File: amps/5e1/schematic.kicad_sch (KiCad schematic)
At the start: 26 parts, among them T1 SE 5k:8

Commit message: Add: real tube pin numbers and readable valve glyphs on every schematic
Phase B of the drawing program. A factory service sheet numbers every tube
pin, because the number is what a technician puts a probe on. This corpus
printed none, and the numbers hidden in its symbols were positional
placeholders (P=1, G=2, K=3) that would have published a 6V6GT's plate as
pin 1 when it is pin 3.

1055 electrodes now carry the real number, 1027 lettered (27 are shared
filaments deduped, 1 dropped for want of clear space on the 6G2). Resolved per
instance from reference/tubes/<slug>.yaml through the same alias resolution the
layout renderer uses, so a 12AX7 section and a 6SL7 section each get their own
basing. A valve whose basing the corpus does not carry prints nothing rather
than a wrong number.

Section letters and basing units are now separate things, which cost a detour
worth recording. The RCA 12AX7-A sheet reads "Pin 1 - Plate of Unit No.2 ...
Pin 6 - Plate of Unit No.1", so unit numbering is not pin order; the 5Y3 and
GZ34 number their units in opposite pin order, so nothing positional can
express it. But the section LETTER is a designator, not a basing fact: this
corpus, like every technician, calls the first stage in signal order V1A, and
five amps' prose already did. On four amps the factory sheets put that first
stage on the other half -- the AA764's own schematic prints +200 V on pin 1 --
so those drawings now state their unit explicitly, each citing its source, and
no letter, netlist, parts list or layout comment changed. 183 layout comments
agree with the printed numbers, 0 disagree. A guard fires if two halves of one
bottle resolve to the same unit, which is exactly how this was found.

Glyphs: the cathode gains a bracket and filament hairpin so it can no longer be
confused with the plate bar, the pentode's screen sits on its own row, and a
rectifier draws as one envelope over its sections instead of two apparent
bottles. Line weights are scaled per sheet to a co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
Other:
- note added: "1"
- note added: "2"
- note added: "2,8"
- note added: "3"
- note added: "4"
- note added: "5"
- note added: "6"
- note added: "7"
- note added: "8"
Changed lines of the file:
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@@
   (wire (pts (xy 41.4116 30.278) (xy 41.4116 38.278))
     (stroke (width 0) (type default)))
-  (junction (at 41.4116 38.278) (diameter 0) (color 0 0 0 0))
+  (junction (at 41.4116 38.278) (diameter 1) (color 0 0 0 0))
   (symbol (lib_id "cx:R") (at 41.4116 42.088 0) (unit 1)
     (in_bom yes) (on_board yes)
@@
   (wire (pts (xy 52.8416 27.178) (xy 60.4616 27.178))
     (stroke (width 0) (type default)))
-  (junction (at 52.8416 27.178) (diameter 0) (color 0 0 0 0))
+  (junction (at 52.8416 27.178) (diameter 1) (color 0 0 0 0))
   (symbol (lib_id "cx:C") (at 64.2716 27.178 90) (unit 1)
     (in_bom yes) (on_board yes)
@@
   (wire (pts (xy 98.5616 45.898) (xy 98.5616 48.278))
     (stroke (width 0) (type default)))
-  (junction (at 98.5616 48.278) (diameter 0) (color 0 0 0 0))
+  (junction (at 98.5616 48.278) (diameter 1) (color 0 0 0 0))
   (symbol (lib_id "cx:R") (at 98.5616 52.088 0) (unit 1)
     (in_bom yes) (on_board yes)
@@
   (wire (pts (xy 98.5616 27.178) (xy 106.182 27.178))
     (stroke (width 0) (type default)))
-  (junction (at 98.5616 27.178) (diameter 0) (color 0 0 0 0))
+  (junction (at 98.5616 27.178) (diameter 1) (color 0 0 0 0))
   (symbol (lib_id "cx:C") (at 109.992 27.178 90) (unit 1)
     (in_bom yes) (on_board yes)
@@
   (wire (pts (xy 118.882 27.178) (xy 118.882 38.278))
     (stroke (width 0) (type default)))
-  (junction (at 118.882 38.278) (diameter 0) (color 0 0 0 0))
+  (junction (at 118.882 38.278) (diameter 1) (color 0 0 0 0))
   (symbol (lib_id "cx:R") (at 118.882 42.088 0) (unit 1)
     (in_bom yes) (on_board yes)
@@
   (wire (pts (xy 55.3816 111.078) (xy 68.0816 111.078))
     (stroke (width 0) (type default)))
-  (junction (at 55.3816 111.078) (diameter 0) (color 0 0 0 0))
-  (junction (at 68.0816 111.078) (diameter 0) (color 0 0 0 0))
+  (junction (at 55.3816 111.078) (diameter 1) (color 0 0 0 0))
+  (junction (at 68.0816 111.078) (diameter 1) (color 0 0 0 0))
   (symbol (lib_id "cx:C") (at 68.0816 114.888 0) (unit 1)
     (in_bom yes) (on_board yes)
@@
   (wire (pts (xy 91.1216 111.078) (xy 98.8816 111.078))
     (stroke (width 0) (type default)))
-  (junction (at 98.8816 111.078) (diameter 0) (color 0 0 0 0))
+  (junction (at 98.8816 111.078) (diameter 1) (color 0 0 0 0))
   (symbol (lib_id "cx:C") (at 98.8816 114.888 0) (unit 1)
     (in_bom yes) (on_board yes)
@@
   (wire (pts (xy 110.502 111.078) (xy 113.882 111.078))
     (stroke (width 0) (type default)))
-  (junction (at 113.882 111.078) (diameter 0) (color 0 0 0 0))
+  (junction (at 113.882 111.078) (diameter 1) (color 0 0 0 0))
   (symbol (lib_id "cx:C") (at 113.882 114.888 0) (unit 1)
     (in_bom yes) (on_board yes)
@@
   (global_label "B+3" (shape input) (at 113.882 107.518 90)
     (effects (font (size 1.27 1.27)) (justify left)))
+  (polyline (pts (xy 55.3816 95.978) (xy 56.3726 96.076) (xy 57.3256 96.365) (xy 58.2036 96.834) (xy 58.9736 97.466) (xy 59.6056 98.236) (xy 60.0746 99.114) (xy 60.3636 100.067) (xy 60.4616 101.058) (xy 60.3636 102.049) (xy 60.0746 103.002) (xy 59.6056 103.88) (xy 58.9736 104.65) (xy 58.2036 105.282) (xy 57.3256 105.751) (xy 56.3726 106.04) (xy 55.3816 106.138) (xy 42.6816 106.138) (xy 41.6906 106.04) (xy 40.7376 105.751) (xy 39.8596 105.282) (xy 39.0896 104.65) (xy 38.4576 103.88) (xy 37.9886 103.002) (xy 37.6996 102.049) (xy 37.6016 101.058) (xy 37.6996 100.067) (xy 37.9886 99.114) (xy 38.4576 98.236) (xy 39.0896 97.466) (xy 39.8596 96.834) (xy 40.7376 96.365) (xy 41.6906 96.076) (xy 42.6816 95.978) (xy 55.3816 95.978))
+    (stroke (width 0.3) (type default) (color 197 163 255 1)) (fill (type none)))
+  (polyline (pts (xy 40.7816 103.293) (xy 42.6816 101.693) (xy 49.0316 103.773) (xy 55.3816 101.693) (xy 57.2816 103.293))
+    (stroke (width 0.3) (type default) (color 197 163 255 1)) (fill (type none)))
+  (text "6" (at 53.6916 31.928 0)
+    (effects (font (size 1.1 1.1)) (justify left)))
+  (text "7" (at 45.8944 36.878 0)
+    (effects (font (size 1.1 1.1)) (justify left)))
+  (text "8" (at 53.6916 44.628 0)
+    (effects (font (size 1.1 1.1)) (justify left)))
+  (text "1" (at 99.4116 31.928 0)
+    (effects (font (size 1.1 1.1)) (justify left)))
+  (text "2" (at 91.6144 36.878 0)
+    (effects (font (size 1.1 1.1)) (justify left)))
+  (text "3" (at 99.4116 44.628 0)
+    (effects (font (size 1.1 1.1)) (justify left)))
+  (text "3" (at 129.892 31.293 0)
+    (effects (font (size 1.1 1.1)) (justify left)))
+  (text "5" (at 122.094 36.878 0)
+    (effects (font (size 1.1 1.1)) (justify left)))
+  (text "4" (at 134.942 35.608 0)
+    (effects (font (size 1.1 1.1)) (justify left)))
+  (text "8" (at 129.892 43.993 0)
+    (effects (font (size 1.1 1.1)) (justify left)))
+  (text "6" (at 43.5316 94.708 0)
+    (effects (font (size 1.1 1.1)) (justify left)))
+  (text "2,8" (at 43.5316 107.408 0)
+    (effects (font (size 1.1 1.1)) (justify left)))
+  (text "4" (at 56.2316 94.708 0)
+    (effects (font (size 1.1 1.1)) (justify left)))
   (text "Power supply — center-tapped HT · 5Y3GT full-wave · choke-filtered · heaters and PT primary omitted" (at 12.7 129.856 0)
     (effects (font (size 1.2 1.2)) (justify left)))

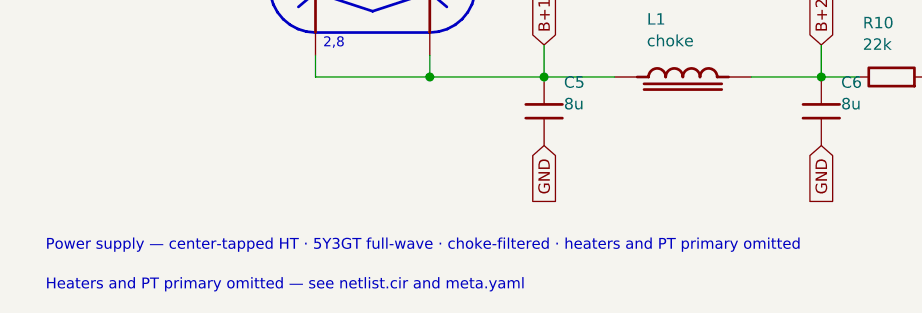
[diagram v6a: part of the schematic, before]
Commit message: Fix: schematic sheet notes no longer name repository files
Thirty-seven committed sheets rendered footnotes and section notes such as
"Heaters and PT primary omitted — see netlist.cir and meta.yaml" or
"excluded from netlist.cir (notes.md)" to visitors through KiCanvas. The
prose sweeps never counted sheets. Rewritten in the site's own words — the
netlist, the sources list, the circuit story, the parts list, the board
drawing — in 59 strings across 33 draw scripts, keeping every technical
claim as it was; the three tone sheets (6G4, 6G5, 6G6-B) are under repair
elsewhere and keep theirs for now. The sweep touched only strings passed to
the sheet's note, text, caption and footnote calls, never a path or a value.

Gates: check_schematics 40/0, connectivity 0 isolated pins;
verify_schematic_nets 40 clean; only the regenerated sheets and their served
copies changed.

Co-Authored-By: Claude Fable 5.1 <noreply@anthropic.com>
Claude-Session: https://claude.ai/code/session_01KBMfdh37HmCL2iWcBiL5J1
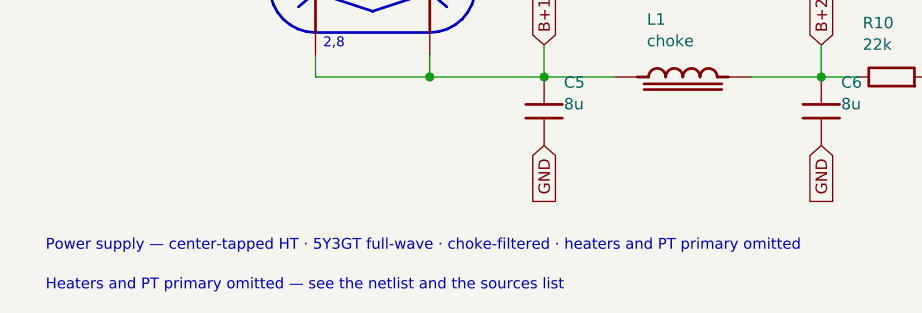
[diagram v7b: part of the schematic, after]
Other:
- note added: "Heaters and PT primary omitted — see the netlist and the sources list"
- note removed: "Heaters and PT primary omitted — see netlist.cir and meta.yaml"
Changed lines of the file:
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@@
   (text "Power supply — center-tapped HT · 5Y3GT full-wave · choke-filtered · heaters and PT primary omitted" (at 12.7 129.856 0)
     (effects (font (size 1.2 1.2)) (justify left)))
-  (text "Heaters and PT primary omitted — see netlist.cir and meta.yaml" (at 12.7 134.256 0)
+  (text "Heaters and PT primary omitted — see the netlist and the sources list" (at 12.7 134.256 0)
     (effects (font (size 1.2 1.2)) (justify left)))
   (sheet_instances (path "/" (page "1")))

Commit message: 5E1: input leak at jack 1's tip, jack side of its 68k (V1 audit)
H-EE hangs the 1 MEG from jack 1's tip on both pages (schematic page
6118x4407 crop 0,1000,1350,1350: jack 1 tip -> 1 MEG -> ground, jack 1's
contact -> ground, jack 2's contact -> jack 1's tip; layout page 5194x4394
crop 3500,600,1300,1900: the 1 MEG from a ground lug to jack 1's tip lug).
The sheet hung it on the grid bus and the board wired it to the V1A grid
pin; both now take it to jack 1's tip. R1 is declared a series_bridge on
both surfaces so the netlist's R3 G1A 0 still binds. BOM role and notes
follow; line-cap role is AC line to chassis on the transformer side of the fuse.
No DC node moves.

Co-Authored-By: Claude Opus 5.5 <noreply@anthropic.com>
Claude-Session: https://claude.ai/code/session_01KBMfdh37HmCL2iWcBiL5J1
Signed-off-by: AnalogMaker <theanalogmaker@gmail.com>
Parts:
- removed C2: .02u, symbol cx:C
- removed V1A: 12AX7, symbol cx:TRIODE
- added R4: 1.5k, symbol cx:R
- added VR1: 1M vol, symbol cx:POT
- C2: renamed from VR1; value 1M vol -> .02u; symbol cx:POT -> cx:C
- V1A: renamed from R4; value 1.5k -> 12AX7; symbol cx:R -> cx:TRIODE
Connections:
- net GND: now also R4.2, VR1.3; no longer C2.3, V1A.2
- net IN 1: now also R3.1
- net at C2.1: now also R5.2, V1A.1 (P)
- net at C2.2: now also VR1.1; no longer V1B.2 (G)
- net at R1.2, R2.2: now also V1A.2 (G); no longer R3.1
- net at C1.1: now also V1A.3 (K), R4.1; no longer V1A.1
- new net: V1B.2 (G), VR1.2 (W)
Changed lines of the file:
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@@
   (global_label "IN 1" (shape input) (at 17.8816 38.278 180)
     (effects (font (size 1.27 1.27)) (justify right)))
-  (wire (pts (xy 17.8816 38.278) (xy 25.1716 38.278))
+  (wire (pts (xy 17.8816 38.278) (xy 21.8816 38.278))
+    (stroke (width 0) (type default)))
+  (wire (pts (xy 21.8816 38.278) (xy 25.1716 38.278))
     (stroke (width 0) (type default)))
   (symbol (lib_id "cx:R") (at 28.9816 38.278 90) (unit 1)
@@
     (stroke (width 0) (type default)))
   (junction (at 41.4116 38.278) (diameter 1) (color 0 0 0 0))
-  (symbol (lib_id "cx:R") (at 41.4116 42.088 0) (unit 1)
+  (junction (at 21.8816 38.278) (diameter 1) (color 0 0 0 0))
+  (symbol (lib_id "cx:R") (at 21.8816 42.088 0) (unit 1)
     (in_bom yes) (on_board yes)
-    (property "Reference" "R3" (at 43.6116 38.888 0) (effects (font (size 1.27 1.27)) (justify left)))
-    (property "Value" "1M" (at 43.6116 41.288 0) (effects (font (size 1.27 1.27)) (justify left))))
-  (global_label "GND" (shape input) (at 41.4116 45.898 270)
+    (property "Reference" "R3" (at 24.0816 42.088 0) (effects (font (size 1.27 1.27)) (justify left)))
+    (property "Value" "1M" (at 24.0816 44.488 0) (effects (font (size 1.27 1.27)) (justify left))))
+  (global_label "GND" (shape input) (at 21.8816 45.898 270)
     (effects (font (size 1.27 1.27)) (justify right)))
   (wire (pts (xy 41.4116 38.278) (xy 45.2216 38.278))
